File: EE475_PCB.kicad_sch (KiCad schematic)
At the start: 6 parts, among them U1 ATSAMD21G18A-M

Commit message: ensure updated
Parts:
- added FB?: FerriteBead_Small, symbol Device:FerriteBead_Small
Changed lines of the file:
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@@
+    (pin "2")
+  )
+  (symbol (lib_id "Device:FerriteBead_Small") (at 45.72 82.55 0) (unit 1)
+    (in_bom yes) (on_board yes) (fields_autoplaced)
+    (property "Reference" "FB?" (id 0) (at 48.26 81.2418 0)
+      (effects (font (size 1.27 1.27)) (justify left))
+    )
+    (property "Value" "FerriteBead_Small" (id 1) (at 48.26 83.7818 0)
+      (effects (font (size 1.27 1.27)) (justify left))
+    )
+    (property "Footprint" "" (id 2) (at 43.942 82.55 90)
+      (effects (font (size 1.27 1.27)) hide)
+    )
+    (property "Datasheet" "~" (id 3) (at 45.72 82.55 0)
+      (effects (font (size 1.27 1.27)) hide)
+    )
+    (pin "1")
     (pin "2")
   )
@@
       (reference "C?") (unit 1) (value "10uF") (footprint "")
     )
+    (path "/9d464c0b-8d05-4c36-9ecd-61205612dba4"
+      (reference "FB?") (unit 1) (value "FerriteBead_Small") (footprint "")
+    )
     (path "/ae5d21b8-b016-470d-88dd-a4e6382d2b5c"

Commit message: add new symbol and footprint library
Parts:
- removed FB?: FerriteBead_Small, symbol Device:FerriteBead_Small
- added FL?: BLM18PG471SN1D, BEADC1608X95N, symbol BLM18PG471SN1D:BLM18PG471SN1D
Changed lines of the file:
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@@
     (stroke (width 0) (type default) (color 0 0 0 0))
+  )
+  (symbol (lib_id "BLM18PG471SN1D:BLM18PG471SN1D") (at 44.45 87.63 270) (unit 1)
+    (in_bom yes) (on_board yes) (fields_autoplaced)
+    (property "Reference" "FL?" (id 0) (at 48.26 85.0899 90)
+      (effects (font (size 1.27 1.27)) (justify left))
+    )
+    (property "Value" "BLM18PG471SN1D" (id 1) (at 48.26 87.6299 90)
+      (effects (font (size 1.27 1.27)) (justify left))
+    )
+    (property "Footprint" "BEADC1608X95N" (id 2) (at 44.45 87.63 0)
+      (effects (font (size 1.27 1.27)) (justify left bottom) hide)
+    )
+    (property "Datasheet" "" (id 3) (at 44.45 87.63 0)
+      (effects (font (size 1.27 1.27)) (justify left bottom) hide)
+    )
+    (pin "1")
+    (pin "2")
   )
   (symbol (lib_id "power:GND") (at 104.14 58.42 0) (unit 1)
@@
     )
     (property "Datasheet" "~" (id 3) (at 102.87 76.2 0)
-      (effects (font (size 1.27 1.27)) hide)
-    )
-    (pin "1")
-    (pin "2")
-  )
-  (symbol (lib_id "Device:FerriteBead_Small") (at 45.72 82.55 0) (unit 1)
-    (in_bom yes) (on_board yes) (fields_autoplaced)
-    (property "Reference" "FB?" (id 0) (at 48.26 81.2418 0)
-      (effects (font (size 1.27 1.27)) (justify left))
-    )
-    (property "Value" "FerriteBead_Small" (id 1) (at 48.26 83.7818 0)
-      (effects (font (size 1.27 1.27)) (justify left))
-    )
-    (property "Footprint" "" (id 2) (at 43.942 82.55 90)
-      (effects (font (size 1.27 1.27)) hide)
-    )
-    (property "Datasheet" "~" (id 3) (at 45.72 82.55 0)
       (effects (font (size 1.27 1.27)) hide)
     )
@@
       (reference "C?") (unit 1) (value "10uF") (footprint "")
     )
-    (path "/9d464c0b-8d05-4c36-9ecd-61205612dba4"
-      (reference "FB?") (unit 1) (value "FerriteBead_Small") (footprint "")
+    (path "/05a7604e-e7e7-4acd-82de-76926ddc4c4c"
+      (reference "FL?") (unit 1) (value "BLM18PG471SN1D") (footprint "BEADC1608X95N")
     )
     (path "/ae5d21b8-b016-470d-88dd-a4e6382d2b5c"

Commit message: include libraries folder
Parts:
- removed FL?: BLM18PG471SN1D, BEADC1608X95N, symbol BLM18PG471SN1D:BLM18PG471SN1D
- added FL?: BLM18PG471SN1D, BEADC1608X95N, symbol BLM18PG471SN1D:BLM18PG471SN1D
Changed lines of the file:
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@@
     (stroke (width 0) (type default) (color 0 0 0 0))
-  )
-  (symbol (lib_id "BLM18PG471SN1D:BLM18PG471SN1D") (at 44.45 87.63 270) (unit 1)
-    (in_bom yes) (on_board yes) (fields_autoplaced)
-    (property "Reference" "FL?" (id 0) (at 48.26 85.0899 90)
-      (effects (font (size 1.27 1.27)) (justify left))
-    )
-    (property "Value" "BLM18PG471SN1D" (id 1) (at 48.26 87.6299 90)
-      (effects (font (size 1.27 1.27)) (justify left))
-    )
-    (property "Footprint" "BEADC1608X95N" (id 2) (at 44.45 87.63 0)
-      (effects (font (size 1.27 1.27)) (justify left bottom) hide)
-    )
-    (property "Datasheet" "" (id 3) (at 44.45 87.63 0)
-      (effects (font (size 1.27 1.27)) (justify left bottom) hide)
-    )
-    (pin "1")
-    (pin "2")
   )
   (symbol (lib_id "power:GND") (at 104.14 58.42 0) (unit 1)
@@
     (pin "1")
   )
+  (symbol (lib_id "BLM18PG471SN1D:BLM18PG471SN1D") (at 44.45 96.52 90) (unit 1)
+    (in_bom yes) (on_board yes) (fields_autoplaced)
+    (property "Reference" "FL?" (id 0) (at 48.26 96.5199 90)
+      (effects (font (size 1.27 1.27)) (justify right))
+    )
+    (property "Value" "BLM18PG471SN1D" (id 1) (at 48.26 99.0599 90)
+      (effects (font (size 1.27 1.27)) (justify right))
+    )
+    (property "Footprint" "BEADC1608X95N" (id 2) (at 44.45 96.52 0)
+      (effects (font (size 1.27 1.27)) (justify left bottom) hide)
+    )
+    (property "Datasheet" "" (id 3) (at 44.45 96.52 0)
+      (effects (font (size 1.27 1.27)) (justify left bottom) hide)
+    )
+    (pin "1")
+    (pin "2")
+  )
   (symbol (lib_id "power:GND") (at 102.87 82.55 0) (unit 1)
     (in_bom yes) (on_board yes) (fields_autoplaced)
@@
       (reference "C?") (unit 1) (value "10uF") (footprint "")
     )
-    (path "/05a7604e-e7e7-4acd-82de-76926ddc4c4c"
+    (path "/dc796718-1625-4fb3-9f21-b6205a53730b"
       (reference "FL?") (unit 1) (value "BLM18PG471SN1D") (footprint "BEADC1608X95N")
     )

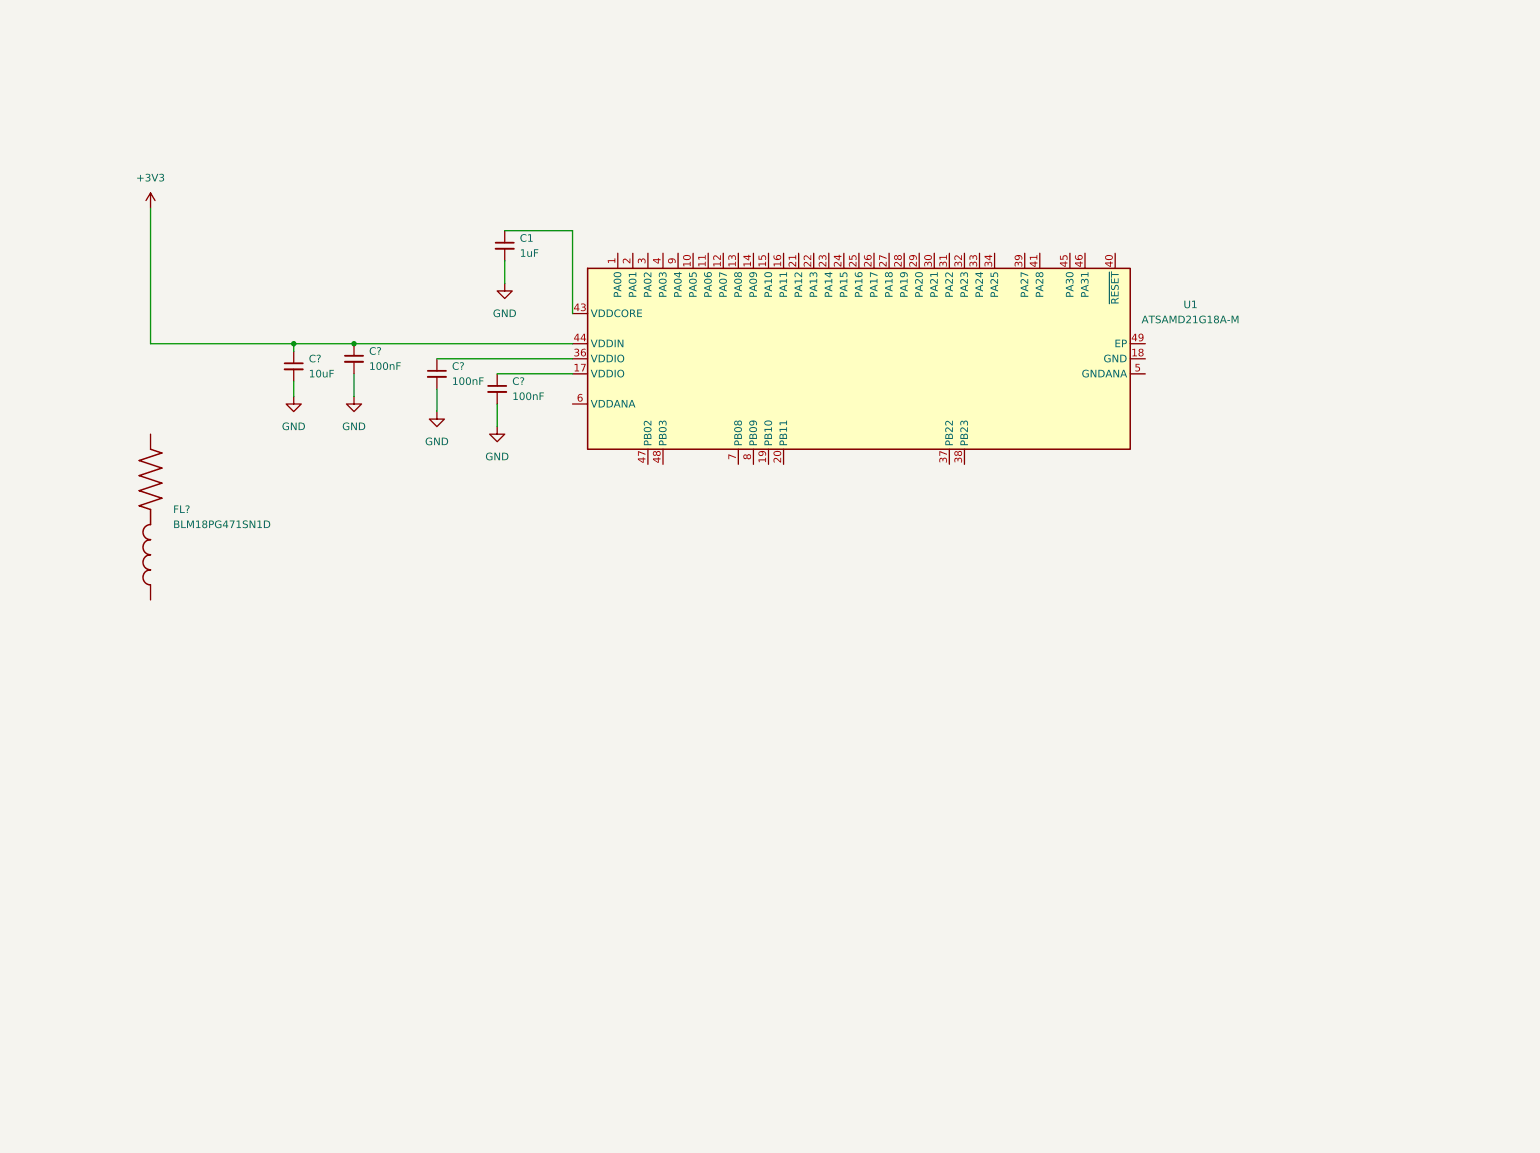
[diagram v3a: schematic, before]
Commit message: Added radio module, step down converter, and labels
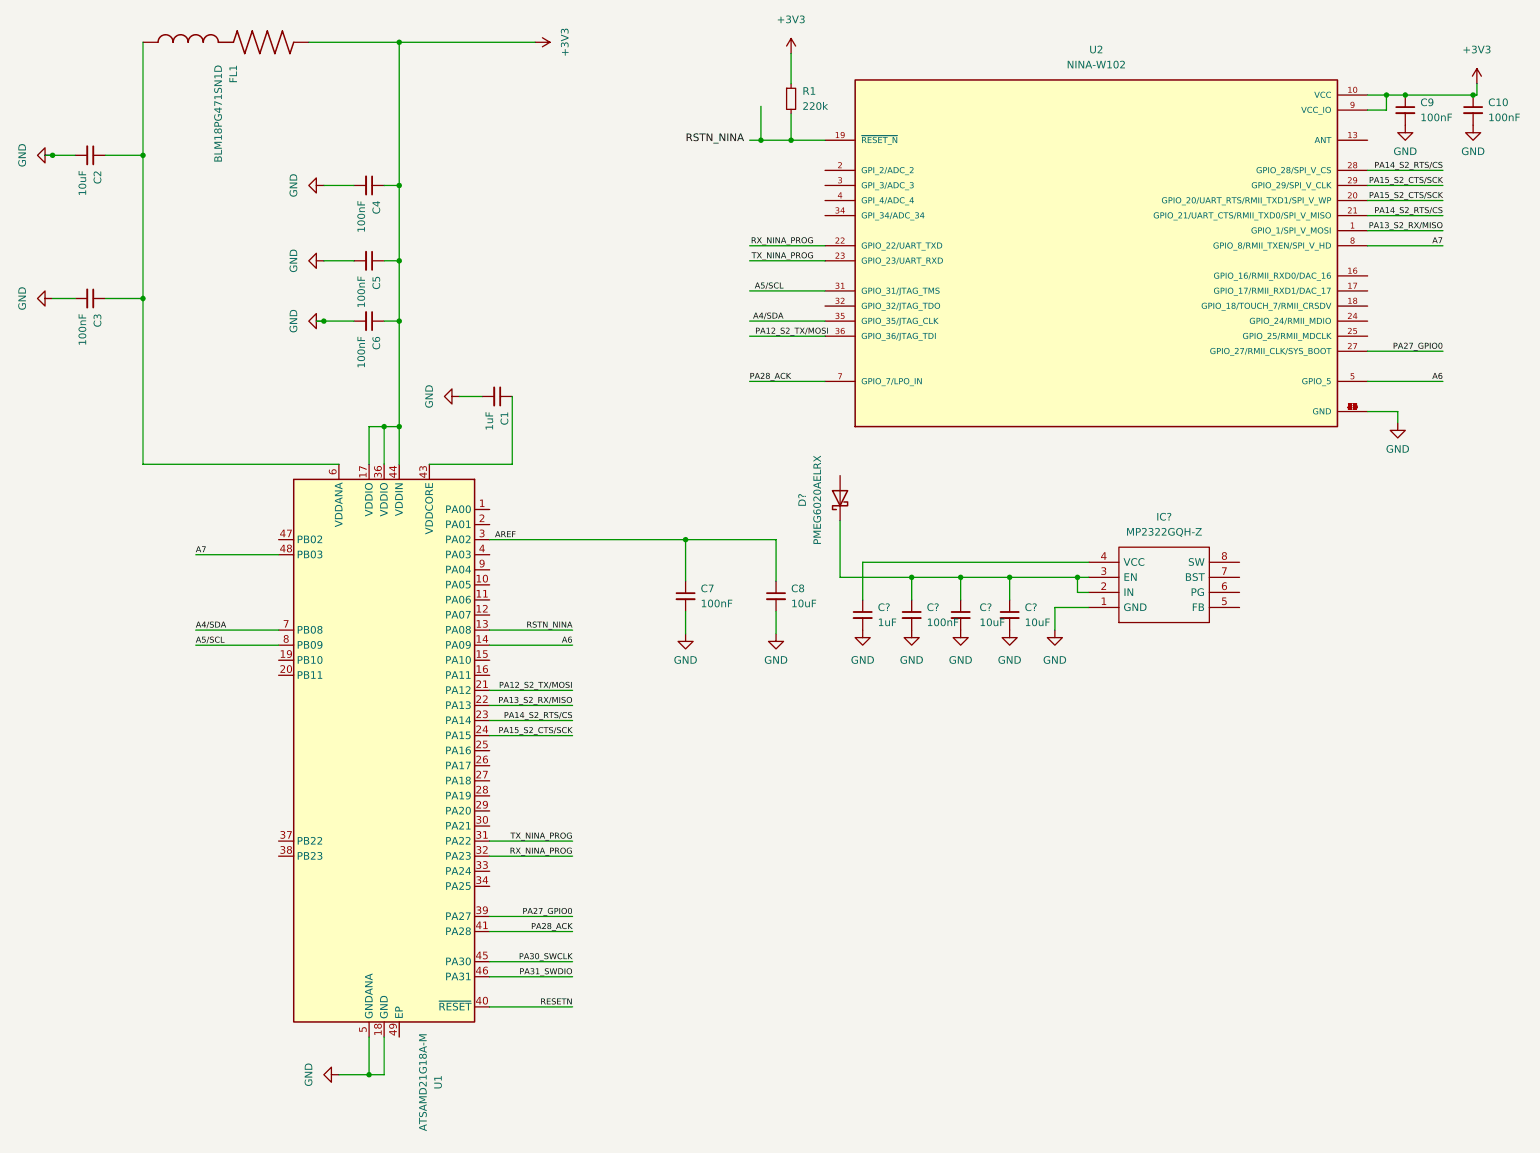
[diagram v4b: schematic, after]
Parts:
- removed C? (x3): 100nF, symbol Device:C_Small
- removed C?: 10uF, symbol Device:C_Small
- added C10, C3, C4, C5, C6, C7, C9, C?: 100nF, symbol Device:C_Small
- added C2, C8, C? (x2): 10uF, symbol Device:C_Small
- added C?: 1uF, symbol Device:C_Small
- added D?: PMEG6020AELRX, symbol Device:D_Schottky
- added IC?: MP2322GQH-Z, MP2322GQHZ, symbol MP2322GQH-Z:MP2322GQH-Z
- added R1: 220k, symbol Device:R_Small
- added U2: NINA-W102, XCVR_NINA-W102, symbol NINA-W102:NINA-W102
- gave numbers to parts that had none: 1
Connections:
- net +3V3: now also FL1.2, U1.17 (VDDIO), U1.36 (VDDIO), C10.1, C4.1, C5.1, C6.1, C9.1, R1.1, U2.10 (VCC), U2.9 (VCC_IO)
- net GND: now also U1.18 (GND), U1.35 (GND), U1.42 (GND), U1.5 (GNDANA), C10.2, C2.2, C3.2, C4.2, C5.2, C6.2, C7.2, C8.2, C9.2, C?.2, C?.2, C?.2, C?.2, IC?.1 (GND), U2.12 (GND), U2.14 (GND), U2.26 (GND), U2.30 (GND), U2.37 (GND), U2.38 (GND), U2.39 (GND), U2.40 (GND), U2.41 (GND), U2.42 (GND), U2.43 (GND), U2.44 (GND), U2.45 (GND), U2.46 (GND), U2.47 (GND), U2.48 (GND), U2.6 (GND)
- net RSTN_NINA: now reaches U1.13 (PA08)
- net A6: now reaches U1.14 (PA09)
- net A6: now also U2.5 (GPIO_5)
- net PA12_S2_TX/MOSI: now reaches U1.21 (PA12)
- net PA13_S2_RX/MISO: now reaches U1.22 (PA13)
- net PA13_S2_RX/MISO: now also U2.1 (GPIO_1/SPI_V_MOSI)
- net PA14_S2_RTS/CS: now reaches U1.23 (PA14)
- net PA14_S2_RTS/CS: now also U2.21 (GPIO_21/UART_CTS/RMII_TXD0/SPI_V_MISO), U2.28 (GPIO_28/SPI_V_CS)
- net PA15_S2_CTS/SCK: now reaches U1.24 (PA15)
- net PA15_S2_CTS/SCK: now also U2.20 (GPIO_20/UART_RTS/RMII_TXD1/SPI_V_WP), U2.29 (GPIO_29/SPI_V_CLK)
- net AREF: now reaches U1.3 (PA02)
- net AREF: now also C7.1, C8.1
- net TX_NINA_PROG: now reaches U1.31 (PA22)
- net TX_NINA_PROG: now also U2.23 (GPIO_23/UART_RXD)
- net RX_NINA_PROG: now reaches U1.32 (PA23)
- net RX_NINA_PROG: now also U2.22 (GPIO_22/UART_TXD)
- net PA27_GPIO0: now reaches U1.39 (PA27)
- net PA27_GPIO0: now also U2.27 (GPIO_27/RMII_CLK/SYS_BOOT)
- net RESETN: now reaches U1.40 (~{RESET})
- net PA28_ACK: now reaches U1.41 (PA28)
- net PA28_ACK: now also U2.7 (GPIO_7/LPO_IN)
- net PA30_SWCLK: now reaches U1.45 (PA30)
- net PA31_SWDIO: now reaches U1.46 (PA31)
- net A7: now reaches U1.48 (PB03)
- net A7: now also U2.8 (GPIO_8/RMII_TXEN/SPI_V_HD)
- net at U1.6 (VDDANA): now also FL1.1, C2.1, C3.1
- net A4/SDA: now reaches U1.7 (PB08)
- net A4/SDA: now also U2.35 (GPIO_35/JTAG_CLK)
- net A5/SCL: now reaches U1.8 (PB09)
- net A5/SCL: now also U2.31 (GPIO_31/JTAG_TMS)
- new net: C?.1, C?.1, C?.1, D?.1 (K), IC?.2 (IN), IC?.3 (EN)
- new net: C?.1, IC?.4 (VCC)
- new net: R1.2, U2.19 (~{RESET_N})
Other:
- moved on the sheet: C1, FL1, U1

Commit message: Update some element's orientation
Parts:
- gave numbers to parts that had none: 6
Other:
- moved on the sheet: C2

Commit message: Updated Schematic for the PCB. Removed the original parts for microcontroller based PCB
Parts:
- removed C1, C11: 1uF, symbol Device:C_Small
- removed C10, C12, C3, C4, C5, C6, C7, C9: 100nF, symbol Device:C_Small
- removed C13, C14, C2, C8: 10uF, symbol Device:C_Small
- removed D1: PMEG6020AELRX, symbol Device:D_Schottky
- removed FL1: BLM18PG471SN1D, BEADC1608X95N, symbol BLM18PG471SN1D:BLM18PG471SN1D
- removed IC1: MP2322GQH-Z, MP2322GQHZ, symbol MP2322GQH-Z:MP2322GQH-Z
- removed R1: 220k, symbol Device:R_Small
- removed U1: ATSAMD21G18A-M, Package_DFN_QFN:QFN-48-1EP_7x7mm_P0.5mm_EP5.15x5.15mm, symbol MCU_Microchip_SAMD:ATSAMD21G18A-M
- removed U2: NINA-W102, XCVR_NINA-W102, symbol NINA-W102:NINA-W102
